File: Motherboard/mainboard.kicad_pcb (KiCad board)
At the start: 4 copper layers, 45 x 35 mm, 48 parts, among them IC1 BMX160, J1 Conn_01x01, J2 10118194-0001LF, J28 Conn_01x01, J29 Conn_01x01, J3 Micro_SD_Card, J30 Conn_01x01, J4 xf2m-2415-1a, J5 XF2M-1015-1A, SW1 KMR231NG LFS, U1 RFM95W-915S2, U2 ATSAMD51G_TQFN48, U3 DRV8848, U4 TPS82740BSIPR, U5 DRV8848, U6 MAX708RESA-T, U8 RFM95W-915S2, X1 ANTENNA_U.FL, X2 ANTENNA_U.FL

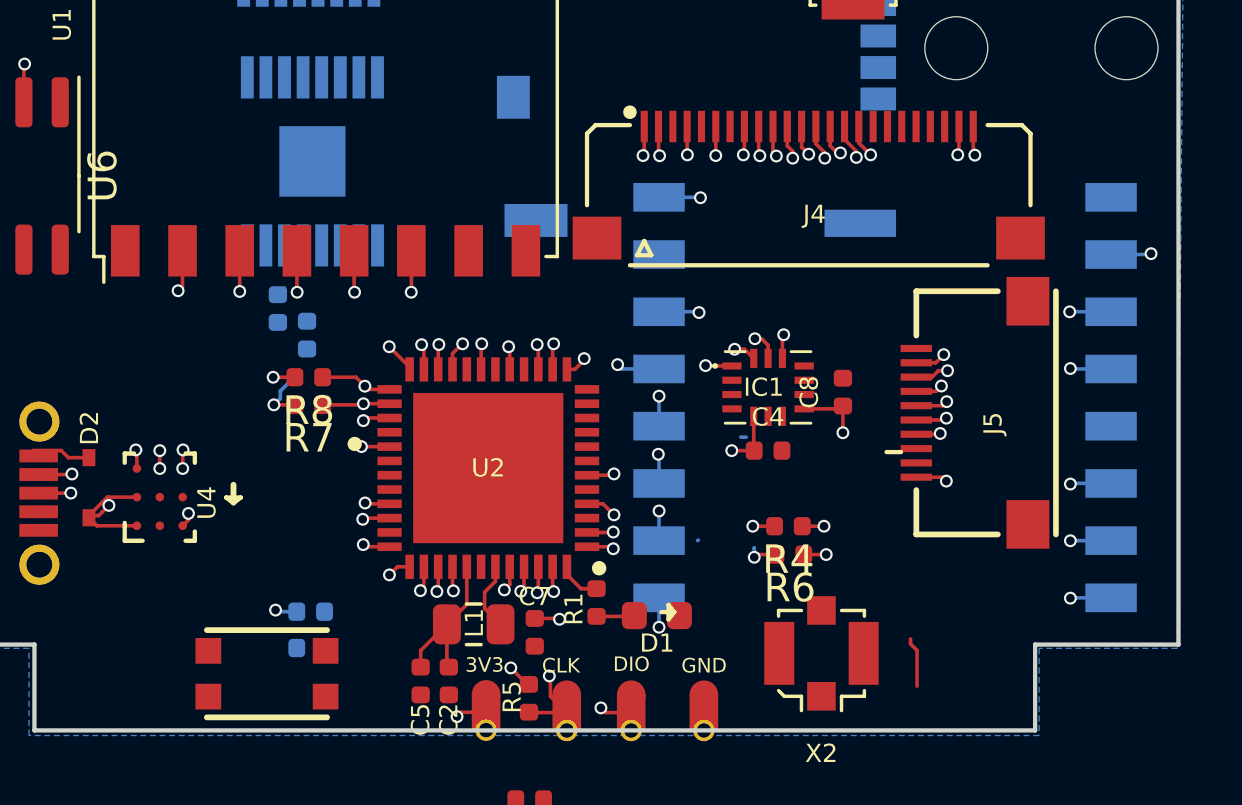
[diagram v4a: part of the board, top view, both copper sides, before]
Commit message: added comm vias and traces to LoRa radio module on top layer
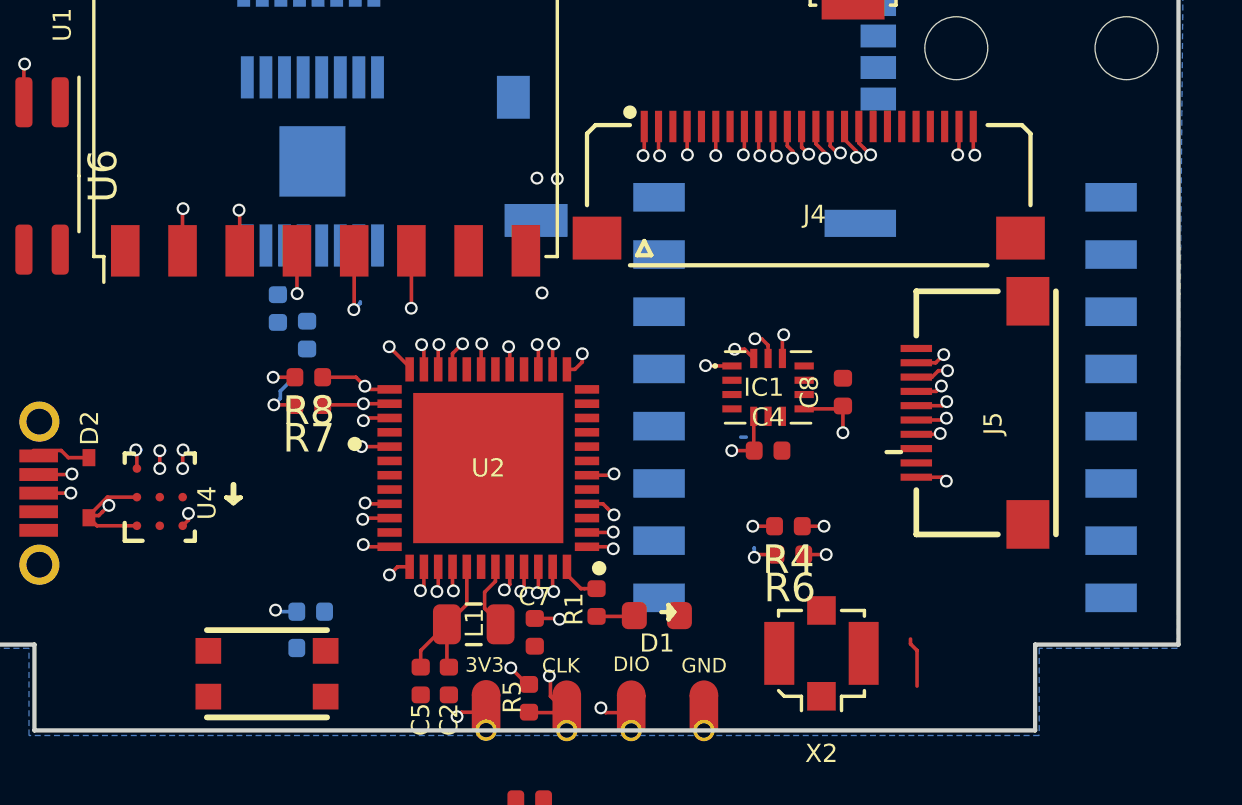
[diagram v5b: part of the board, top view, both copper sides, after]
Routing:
- net WDT_WDI: track 2.27 -> 26.5 mm
- net MISO: track 20.6 -> 38.7 mm
- net MOSI: track 18.4 -> 35.6 mm
- net SCK: track 25.6 -> 35.1 mm
- net GND: track 4.68 -> 0.79 mm, vias 4 -> 1
- net CS_RF1: track 1.51 -> 0.00 mm, vias 1 -> 0
- net RF_DIO3: track 2.35 -> 0.90 mm, vias 2 -> 1
- net RF_DIO0: track 2.32 -> 0.88 mm, vias 2 -> 1
- net RF_BUSY: track 2.31 -> 0.88 mm, vias 2 -> 1
- net RF_DIO2: track 4.05 -> 2.62 mm, vias 2 -> 1
- net RF_DIO1: track 2.31 -> 0.88 mm, vias 2 -> 1
- net RF_RST: track 2.46 -> 1.05 mm, vias 2 -> 1
- net CS_RF2: track 1.45 -> 2.43 mm
- net RF2_RST: track 1.45 -> 2.01 mm

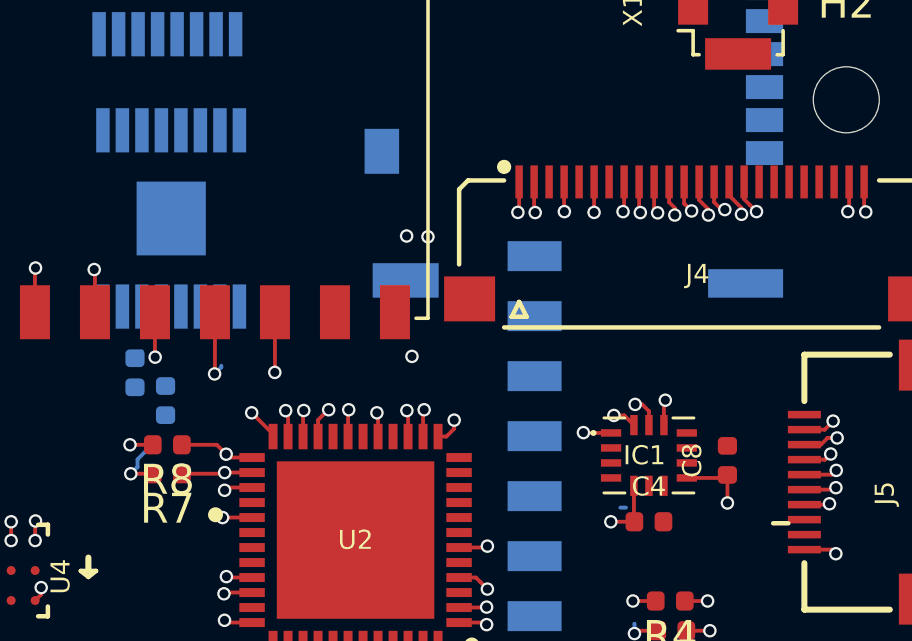
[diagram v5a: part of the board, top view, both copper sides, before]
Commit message: added SCL2 and SDA2 traces between MCU and flat flex connector
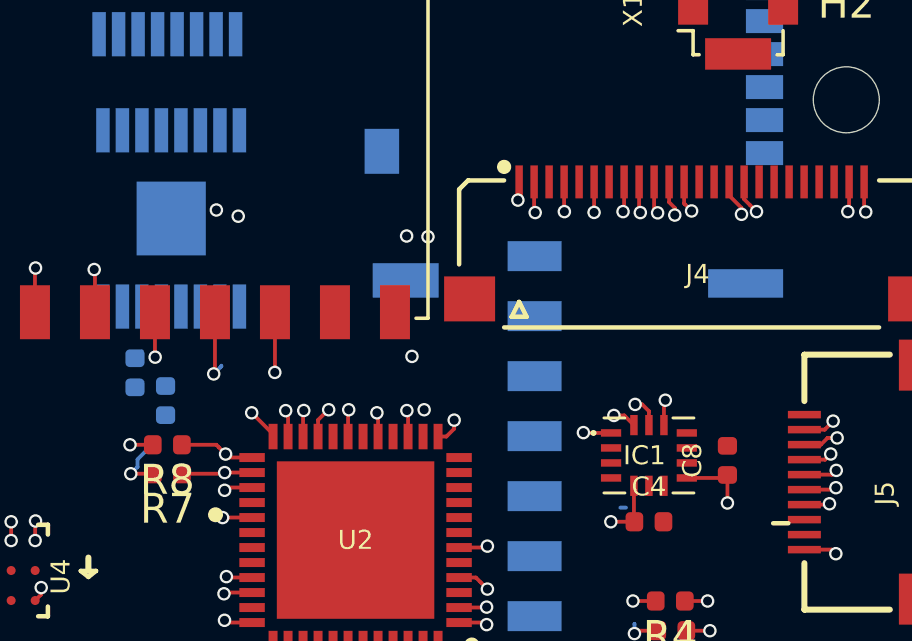
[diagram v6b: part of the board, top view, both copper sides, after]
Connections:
- J4 pad 1: 3V3 -> SCL2
- J4 pad 13: SCL2 -> Net-(J4-Pad13)
- J4 pad 14: SDA2 -> Net-(J4-Pad14)
- J4 pad 2: COIL1P -> SDA2
- J4 pad 21: Net-(J4-Pad21) -> GND
- J4 pad 22: Net-(J4-Pad22) -> 3V3
- J4 pad 3: GND -> COIL1P
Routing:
- net SDA2: track 3.55 -> 22.1 mm, vias 2 -> 3
- net SCL2: track 3.75 -> 21.6 mm, vias 2 -> 3
- net SCK: track 35.1 -> 28.4 mm
- net COIL1P: track 1.04 -> 0.00 mm, vias 1 -> 0
- net 3V3: track 1.03 -> 0.00 mm, vias 1 -> 0
- net MISO: track 38.7 -> 38.0 mm

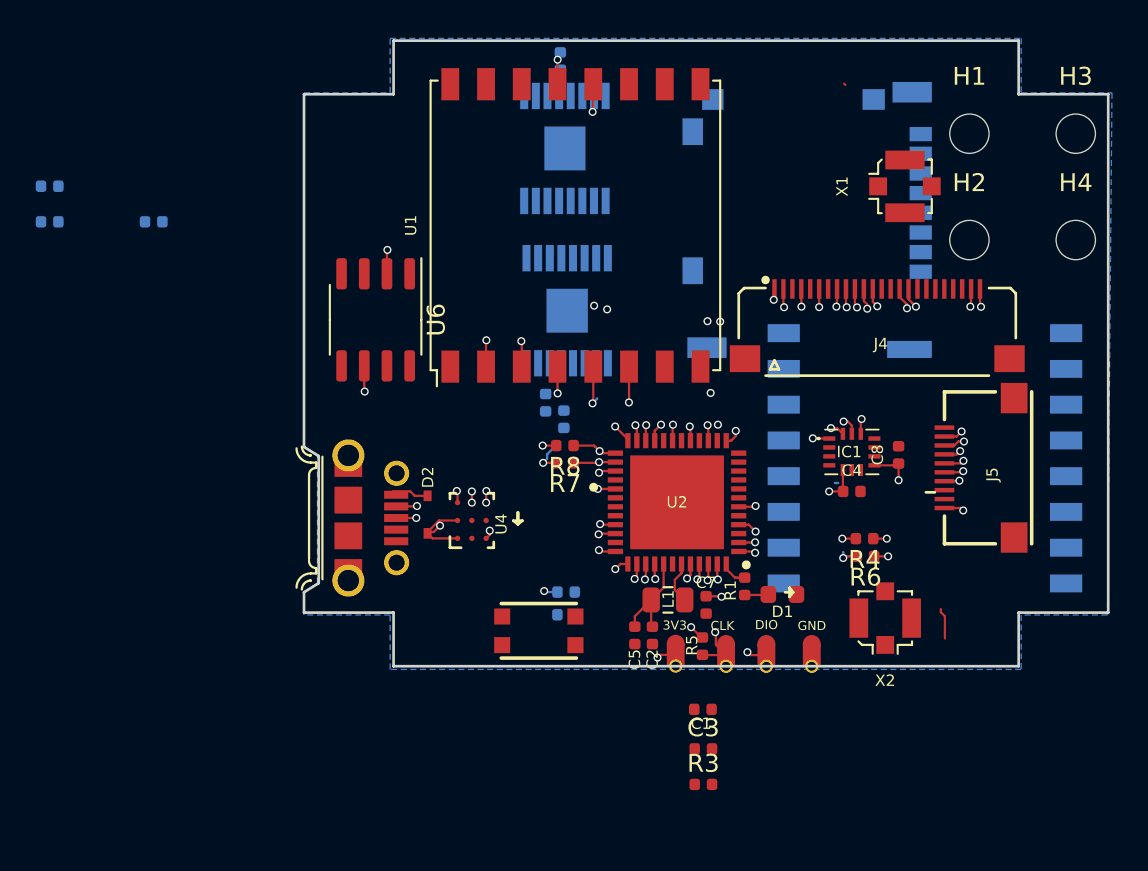
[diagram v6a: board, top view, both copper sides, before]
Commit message: updated location of USB and watchdog timer on top layer, connected watchdog timer to R3 and reset nest on MCU
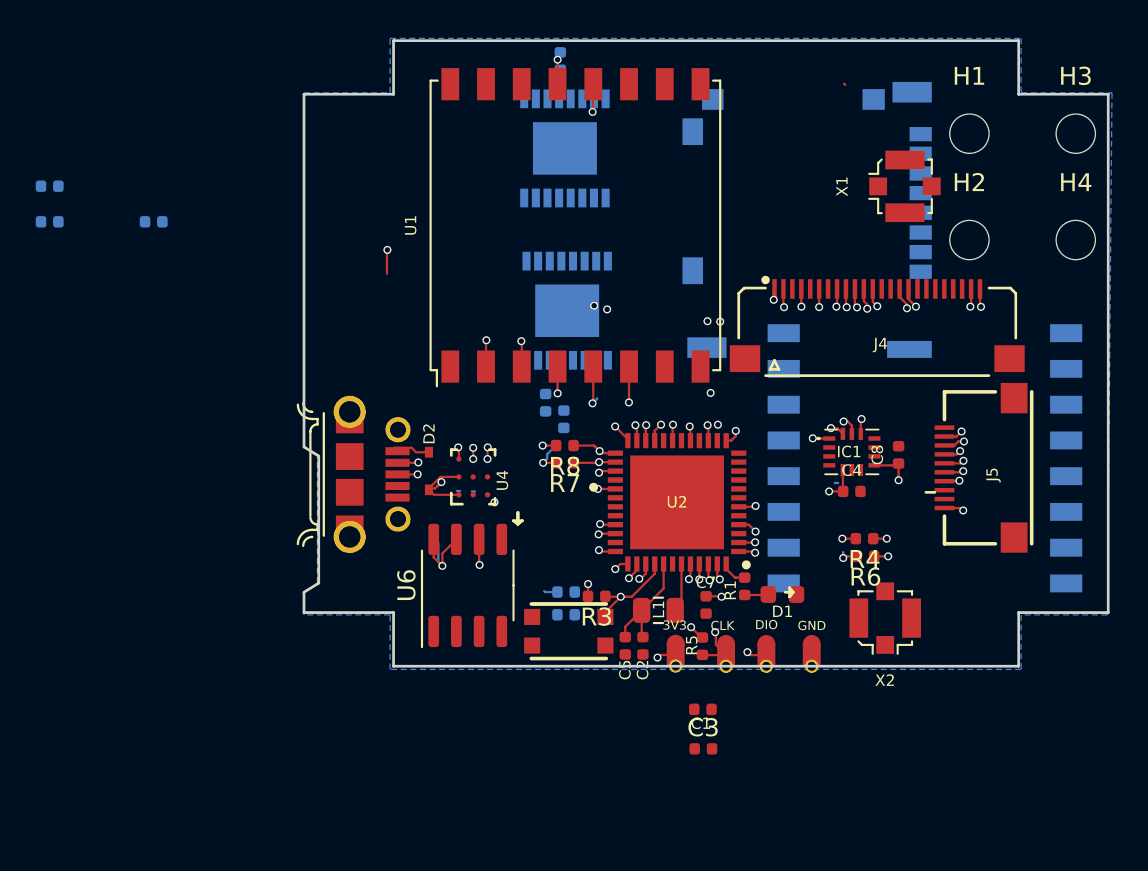
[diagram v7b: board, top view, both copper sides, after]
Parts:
- C12, C9: value 0.1uF -> 100 nF
- U3, U5: footprint KiCAD Libraries:SOP65P640X120-17N -> Package_SO:TSSOP-16-1EP_4.4x5mm_P0.65mm
- moved U6 15.7 mm to (85.9, 104.5), turned to 90 degrees
- moved R3 12.1 mm to (93.1, 105.1), turned to 180 degrees
- moved D2 2.44 mm to (83.7, 98.1)
- moved J2 2.44 mm to (79.3, 98.3)
- moved U4 2.44 mm to (86.2, 98.5)
- moved SW1 1.68 mm to (91.5, 107.1), turned to 0 degrees
- moved L1 0.79 mm to (96.5, 105.9)
- moved C2 0.79 mm to (95.7, 107.9)
- moved C5 0.79 mm to (94.7, 107.9)
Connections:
- J4 pad 1: SCL2 -> 3V3
- J4 pad 13: Net-(J4-Pad13) -> SCL1
- J4 pad 14: Net-(J4-Pad14) -> SCL2
- J4 pad 15: SCL1 -> SDA1
- J4 pad 16: SDA1 -> SDA2
- J4 pad 2: SDA2 -> COIL1P
- J4 pad 21: GND -> Net-(J4-Pad21)
- J4 pad 22: 3V3 -> Net-(J4-Pad22)
- J4 pad 23: BATT_N -> Net-(J4-Pad23)
- J4 pad 24: BATT_P -> Net-(J4-Pad24)
- J4 pad 3: COIL1P -> GND
- J4 pad 5: Net-(J4-Pad5) -> BATT_P
- J4 pad 7: Net-(J4-Pad7) -> BATT_N
- J5 pad 10: Net-(J5-Pad10) -> EN_CAM
- J5 pad 3: Net-(J5-Pad3) -> MOSI
- J5 pad 5: EN_CAM -> CS_CAM
- J5 pad 6: CS_CAM -> Net-(J5-Pad6)
- J5 pad 8: MOSI -> Net-(J5-Pad8)
- U2 pad 27: CS_IMU -> Net-(U2-Pad27)
- U2 pad 37: WDT_WDI -> Net-(U2-Pad37)
- U3 pad 2: MOX_1 -> MINX_1
- U3 pad 4: MOX_2 -> MINX_2
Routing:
- net WDT_WDI: track 26.5 -> 9.95 mm
- net Net-(R3-Pad2): track 0.00 -> 14.3 mm, vias 0 -> 2
- net ~RESET: track 0.86 -> 5.69 mm
- net RF_DIO2: track 2.62 -> 0.98 mm
- net /USB-: track 13.6 -> 14.8 mm
- net /USB+: track 12.9 -> 13.8 mm
- net Net-(C2-Pad1): track 5.70 -> 6.50 mm
- net +3V3: track 20.2 -> 19.6 mm
- net GND: vias 1 -> 0

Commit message: updated board outline to match re-location of USB
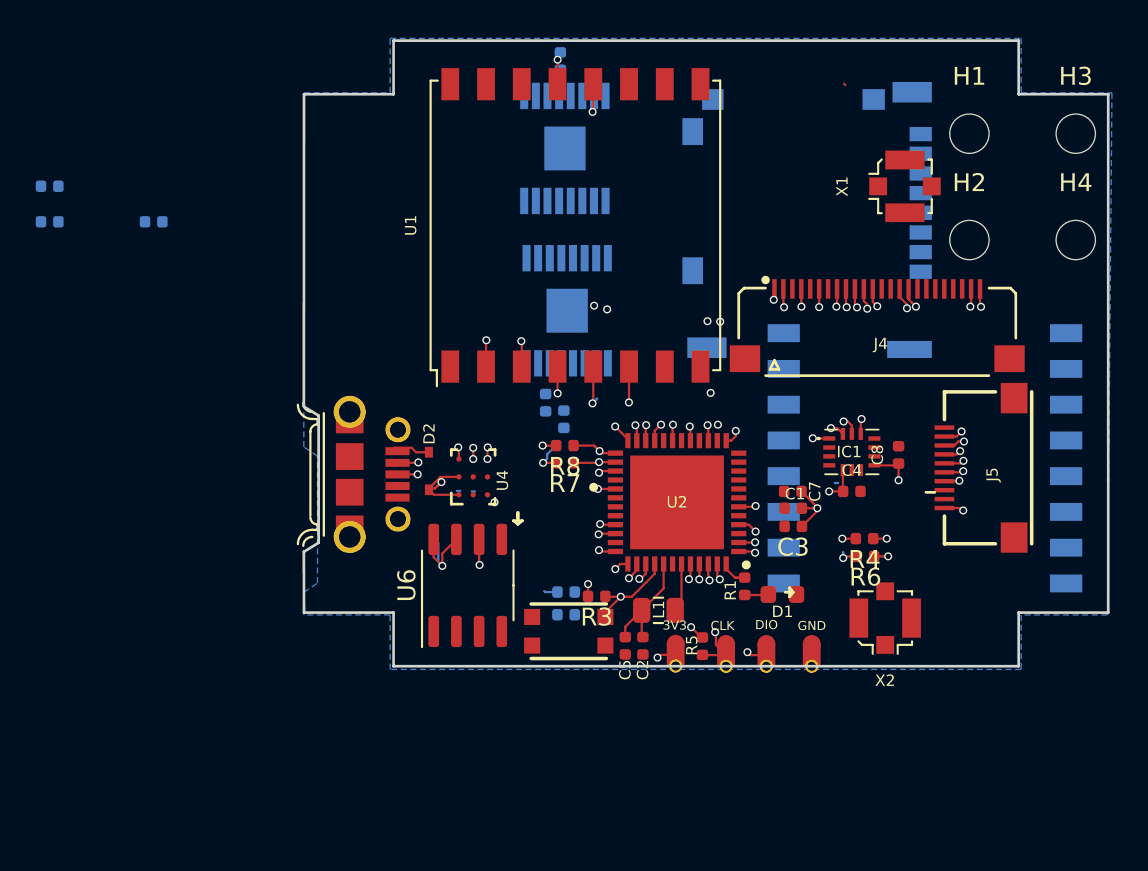
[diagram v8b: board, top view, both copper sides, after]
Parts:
- C12, C9: value 100 nF -> 0.1uF
- U3, U5: footprint Package_SO:TSSOP-16-1EP_4.4x5mm_P0.65mm -> KiCAD Libraries:SOP65P640X120-17N
- moved C3 13.4 mm to (104.1, 101.2), turned to 180 degrees
- moved C1 12.3 mm to (104.1, 100.2), turned to 180 degrees
- moved C7 7.99 mm to (104.1, 99.3), turned to 180 degrees
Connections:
- J4 pad 1: 3V3 -> SCL2
- J4 pad 13: SCL1 -> Net-(J4-Pad13)
- J4 pad 14: SCL2 -> Net-(J4-Pad14)
- J4 pad 15: SDA1 -> SCL1
- J4 pad 16: SDA2 -> SDA1
- J4 pad 2: COIL1P -> SDA2
- J4 pad 21: Net-(J4-Pad21) -> GND
- J4 pad 22: Net-(J4-Pad22) -> 3V3
- J4 pad 23: Net-(J4-Pad23) -> BATT_N
- J4 pad 24: Net-(J4-Pad24) -> BATT_P
- J4 pad 3: GND -> COIL1P
- J4 pad 5: BATT_P -> Net-(J4-Pad5)
- J4 pad 7: BATT_N -> Net-(J4-Pad7)
- J5 pad 10: EN_CAM -> Net-(J5-Pad10)
- J5 pad 3: MOSI -> Net-(J5-Pad3)
- J5 pad 5: CS_CAM -> EN_CAM
- J5 pad 6: Net-(J5-Pad6) -> CS_CAM
- J5 pad 8: Net-(J5-Pad8) -> MOSI
- U2 pad 27: Net-(U2-Pad27) -> CS_IMU
- U2 pad 37: Net-(U2-Pad37) -> WDT_WDI
- U3 pad 2: MINX_1 -> MOX_1
- U3 pad 4: MINX_2 -> MOX_2
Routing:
- net +3V3: track 19.6 -> 21.0 mm, vias 17 -> 16
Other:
- outline, holes or cut-outs redrawn
